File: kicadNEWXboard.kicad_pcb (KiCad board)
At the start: 2 copper layers, 89.7 x 38.1 mm, 24 parts, among them SW1 SW_Push, U1 ATmega32U4-AU, Y1 16MHz

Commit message: SVG
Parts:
- added D10: SOD-123, Diode_SMD:D_SOD-123, B.Cu at (71.3, 112.0)
- added D11: SOD-123, Diode_SMD:D_SOD-123, B.Cu at (90.4, 35.9)
- added D12: SOD-123, Diode_SMD:D_SOD-123, B.Cu at (90.5, 54.8)
- added D13: SOD-123, Diode_SMD:D_SOD-123, B.Cu at (100.0, 73.9)
- added D14: SOD-123, Diode_SMD:D_SOD-123, B.Cu at (90.4, 92.8)
- added D15: SOD-123, Diode_SMD:D_SOD-123, B.Cu at (90.4, 112.0)
- added D16: SOD-123, Diode_SMD:D_SOD-123, B.Cu at (109.4, 35.8)
- added D17: SOD-123, Diode_SMD:D_SOD-123, B.Cu at (109.5, 54.7)
- added D18: SOD-123, Diode_SMD:D_SOD-123, B.Cu at (118.9, 73.8)
- added D19: SOD-123, Diode_SMD:D_SOD-123, B.Cu at (109.4, 92.9)
- added D20: SOD-123, Diode_SMD:D_SOD-123, B.Cu at (114.2, 112.0)
- added D21: SOD-123, Diode_SMD:D_SOD-123, B.Cu at (128.5, 35.8)
- added D22: SOD-123, Diode_SMD:D_SOD-123, B.Cu at (128.5, 54.8)
- added D23: SOD-123, Diode_SMD:D_SOD-123, B.Cu at (138.0, 73.9)
- added D24: SOD-123, Diode_SMD:D_SOD-123, B.Cu at (128.5, 92.8)
- added D25: SOD-123, Diode_SMD:D_SOD-123, B.Cu at (138.0, 112.0)
- added D26: SOD-123, Diode_SMD:D_SOD-123, B.Cu at (147.5, 35.8)
- added D27: SOD-123, Diode_SMD:D_SOD-123, B.Cu at (147.5, 54.8)
- added D28: SOD-123, Diode_SMD:D_SOD-123, B.Cu at (157.0, 73.9)
- added D29: SOD-123, Diode_SMD:D_SOD-123, B.Cu at (147.5, 92.9)
- added D30: SOD-123, Diode_SMD:D_SOD-123, B.Cu at (161.7, 111.9)
- added D31: SOD-123, Diode_SMD:D_SOD-123, B.Cu at (166.6, 35.8)
- added D32: SOD-123, Diode_SMD:D_SOD-123, B.Cu at (166.6, 54.8)
- added D33: SOD-123, Diode_SMD:D_SOD-123, B.Cu at (176.1, 73.9)
- added D34: SOD-123, Diode_SMD:D_SOD-123, B.Cu at (166.7, 92.9)
- added D35: SOD-123, Diode_SMD:D_SOD-123, B.Cu at (185.6, 112.0)
- added D36: SOD-123, Diode_SMD:D_SOD-123, B.Cu at (185.6, 35.8)
- added D37: SOD-123, Diode_SMD:D_SOD-123, B.Cu at (185.6, 54.8)
- added D38: SOD-123, Diode_SMD:D_SOD-123, B.Cu at (195.0, 73.8)
- added D39: SOD-123, Diode_SMD:D_SOD-123, B.Cu at (185.6, 92.9)
- added D40: SOD-123, Diode_SMD:D_SOD-123, B.Cu at (204.7, 112.0)
- added D41: SOD-123, Diode_SMD:D_SOD-123, B.Cu at (204.7, 35.8)
- added D42: SOD-123, Diode_SMD:D_SOD-123, B.Cu at (204.7, 54.8)
- added D43: SOD-123, Diode_SMD:D_SOD-123, B.Cu at (214.2, 73.9)
- added D44: SOD-123, Diode_SMD:D_SOD-123, B.Cu at (204.7, 92.9)
- added D45: SOD-123, Diode_SMD:D_SOD-123, B.Cu at (223.7, 112.0)
- added D46: SOD-123, Diode_SMD:D_SOD-123, B.Cu at (223.7, 35.8)
- added D47: SOD-123, Diode_SMD:D_SOD-123, B.Cu at (223.7, 54.8)
- added D48: SOD-123, Diode_SMD:D_SOD-123, B.Cu at (223.7, 92.9)
- added D5: SOD-123, Diode_SMD:D_SOD-123, B.Cu at (61.9, 73.9)
- added D6: SOD-123, Diode_SMD:D_SOD-123, B.Cu at (52.3, 92.9)
- added D7: SOD-123, Diode_SMD:D_SOD-123, B.Cu at (52.3, 112.0)
- added D8: SOD-123, Diode_SMD:D_SOD-123, B.Cu at (80.8, 73.8)
- added D9: SOD-123, Diode_SMD:D_SOD-123, B.Cu at (71.3, 92.8)
- added MX10: MX-NoLED, MX_Alps_Hybrid:MX-1U, F.Cu at (63.5, 111.9)
- added MX11: MX-NoLED, MX_Alps_Hybrid:MX-1U, F.Cu at (82.5, 35.7)
- added MX12: MX-NoLED, MX_Alps_Hybrid:MX-1U, F.Cu at (82.5, 54.8)
- added MX13: MX-NoLED, MX_Alps_Hybrid:MX-1U, F.Cu at (92.1, 73.8)
- added MX14: MX-NoLED, MX_Alps_Hybrid:MX-1U, F.Cu at (82.5, 92.9)
- added MX15: MX-NoLED, MX_Alps_Hybrid:MX-1U, F.Cu at (82.5, 111.9)
- added MX16: MX-NoLED, MX_Alps_Hybrid:MX-1U, F.Cu at (101.6, 35.7)
- added MX17: MX-NoLED, MX_Alps_Hybrid:MX-1U, F.Cu at (101.6, 54.8)
- added MX18: MX-NoLED, MX_Alps_Hybrid:MX-1U, F.Cu at (111.1, 73.8)
- added MX19: MX-NoLED, MX_Alps_Hybrid:MX-1U, F.Cu at (101.6, 92.9)
- added MX20: MX-NoLED, MX_Alps_Hybrid:MX-1U, F.Cu at (106.4, 111.9)
- added MX21: MX-NoLED, MX_Alps_Hybrid:MX-1U, F.Cu at (120.7, 35.7)
- added MX22: MX-NoLED, MX_Alps_Hybrid:MX-1U, F.Cu at (120.7, 54.8)
- added MX23: MX-NoLED, MX_Alps_Hybrid:MX-1U, F.Cu at (130.2, 73.8)
- added MX24: MX-NoLED, MX_Alps_Hybrid:MX-1U, F.Cu at (120.7, 92.9)
- added MX25: MX-NoLED, MX_Alps_Hybrid:MX-1U, F.Cu at (130.2, 111.9)
- added MX26: MX-NoLED, MX_Alps_Hybrid:MX-1U, F.Cu at (139.7, 35.7)
- added MX27: MX-NoLED, MX_Alps_Hybrid:MX-1U, F.Cu at (139.7, 54.8)
- added MX28: MX-NoLED, MX_Alps_Hybrid:MX-1U, F.Cu at (149.2, 73.8)
- added MX29: MX-NoLED, MX_Alps_Hybrid:MX-1U, F.Cu at (139.7, 92.9)
- added MX30: MX-NoLED, MX_Alps_Hybrid:MX-1U, F.Cu at (154.0, 111.9)
- added MX31: MX-NoLED, MX_Alps_Hybrid:MX-1U, F.Cu at (158.8, 35.7)
- added MX32: MX-NoLED, MX_Alps_Hybrid:MX-1U, F.Cu at (158.8, 54.8)
- added MX33: MX-NoLED, MX_Alps_Hybrid:MX-1U, F.Cu at (168.3, 73.8)
- added MX34: MX-NoLED, MX_Alps_Hybrid:MX-1U, F.Cu at (158.8, 92.9)
- added MX35: MX-NoLED, MX_Alps_Hybrid:MX-1U, F.Cu at (177.8, 111.9)
- added MX36: MX-NoLED, MX_Alps_Hybrid:MX-1U, F.Cu at (177.8, 35.7)
- added MX37: MX-NoLED, MX_Alps_Hybrid:MX-1U, F.Cu at (177.8, 54.8)
- added MX38: MX-NoLED, MX_Alps_Hybrid:MX-1U, F.Cu at (187.3, 73.8)
- added MX39: MX-NoLED, MX_Alps_Hybrid:MX-1U, F.Cu at (177.8, 92.9)
- added MX40: MX-NoLED, MX_Alps_Hybrid:MX-1U, F.Cu at (196.8, 111.9)
- added MX41: MX-NoLED, MX_Alps_Hybrid:MX-1U, F.Cu at (196.8, 35.7)
- added MX42: MX-NoLED, MX_Alps_Hybrid:MX-1U, F.Cu at (196.8, 54.8)
- added MX43: MX-NoLED, MX_Alps_Hybrid:MX-1U, F.Cu at (206.4, 73.8)
- added MX44: MX-NoLED, MX_Alps_Hybrid:MX-1U, F.Cu at (196.8, 92.9)
- added MX45: MX-NoLED, MX_Alps_Hybrid:MX-1U, F.Cu at (215.9, 111.9)
- added MX46: MX-NoLED, MX_Alps_Hybrid:MX-1U, F.Cu at (215.9, 35.7)
- added MX47: MX-NoLED, MX_Alps_Hybrid:MX-1U, F.Cu at (215.9, 54.8)
- added MX48: MX-NoLED, MX_Alps_Hybrid:MX-1U, F.Cu at (215.9, 92.9)
- added MX5: MX-NoLED, MX_Alps_Hybrid:MX-1U, F.Cu at (54.0, 73.8)
- added MX6: MX-NoLED, MX_Alps_Hybrid:MX-1U, F.Cu at (44.5, 92.9)
- added MX7: MX-NoLED, MX_Alps_Hybrid:MX-1U, F.Cu at (44.5, 111.9)
- added MX8: MX-NoLED, MX_Alps_Hybrid:MX-1U, F.Cu at (73.0, 73.8)
- added MX9: MX-NoLED, MX_Alps_Hybrid:MX-1U, F.Cu at (63.5, 92.9)
- moved MX3 152.9 mm to (63.5, 35.7)
- moved MX4 152.9 mm to (63.5, 54.8)
- moved MX1 152.9 mm to (44.5, 35.7)
- moved MX2 152.9 mm to (44.5, 54.8)
- moved D4 138.3 mm to (71.4, 54.8)
- moved D1 138.1 mm to (52.4, 35.8)
- moved D3 138.1 mm to (71.4, 35.8)
- moved D2 137.9 mm to (52.4, 54.8)
- moved USB1 105.4 mm to (223.6, 134.5), turned to 180 degrees
- moved R1 96.6 mm to (210.4, 149.2), turned to 180 degrees
- moved SW1 93.6 mm to (220.9, 147.4), turned to 270 degrees
- moved R2 90.5 mm to (210.4, 145.5), turned to 180 degrees
- moved F1 90.5 mm to (211.3, 138.7), turned to 0 degrees
- moved R3 74.3 mm to (188.2, 154.6), turned to 180 degrees
- moved C6 70.5 mm to (193.2, 153.4)
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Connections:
- U1 pad 18: Net-(U1-Pad18) -> COL0
- U1 pad 19: Net-(U1-Pad19) -> COL1
- U1 pad 20: Net-(U1-Pad20) -> COL2
- U1 pad 21: Net-(U1-Pad21) -> COL3
- U1 pad 22: Net-(U1-Pad22) -> COL4
- U1 pad 26: Net-(U1-Pad26) -> COL5
- U1 pad 27: Net-(U1-Pad27) -> COL6
- U1 pad 28: Net-(U1-Pad28) -> COL7
- U1 pad 29: Net-(U1-Pad29) -> COL8
- U1 pad 30: Net-(U1-Pad30) -> COL9
- U1 pad 37: Net-(U1-Pad37) -> ROW0
- U1 pad 38: Net-(U1-Pad38) -> ROW1
- U1 pad 39: Net-(U1-Pad39) -> ROW2
- U1 pad 40: Net-(U1-Pad40) -> ROW3
- U1 pad 41: Net-(U1-Pad41) -> ROW4
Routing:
- net ROW0: track 19.6 -> 303.5 mm, vias 0 -> 6
- net COL2: track 0.00 -> 227.0 mm, vias 0 -> 1
- net ROW4: track 0.00 -> 220.8 mm, vias 0 -> 4
- net COL0: track 38.5 -> 256.6 mm, vias 0 -> 1
- net COL1: track 29.3 -> 236.8 mm, vias 0 -> 1
- net COL3: track 0.00 -> 195.1 mm, vias 0 -> 1
- net COL4: track 0.00 -> 173.6 mm, vias 0 -> 1
- net COL5: track 0.00 -> 155.6 mm, vias 0 -> 3
- net COL6: track 0.00 -> 132.9 mm, vias 0 -> 1
- net COL8: track 0.00 -> 129.7 mm, vias 0 -> 2
- net COL7: track 0.00 -> 125.4 mm, vias 0 -> 1
- net COL9: track 0.00 -> 110.8 mm, vias 0 -> 2
- net ROW2: track 0.00 -> 85.1 mm, vias 0 -> 6
- net ROW1: track 20.0 -> 101.9 mm, vias 0 -> 6
- net ROW3: track 0.00 -> 63.9 mm, vias 0 -> 6
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- added copper zone on B.Cu, net GND
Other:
- board size 89.7 x 38.1 mm -> 190.5 x 131.8 mm
- board text added: "newk-board-01 so cool and so awesome wow wow wow"

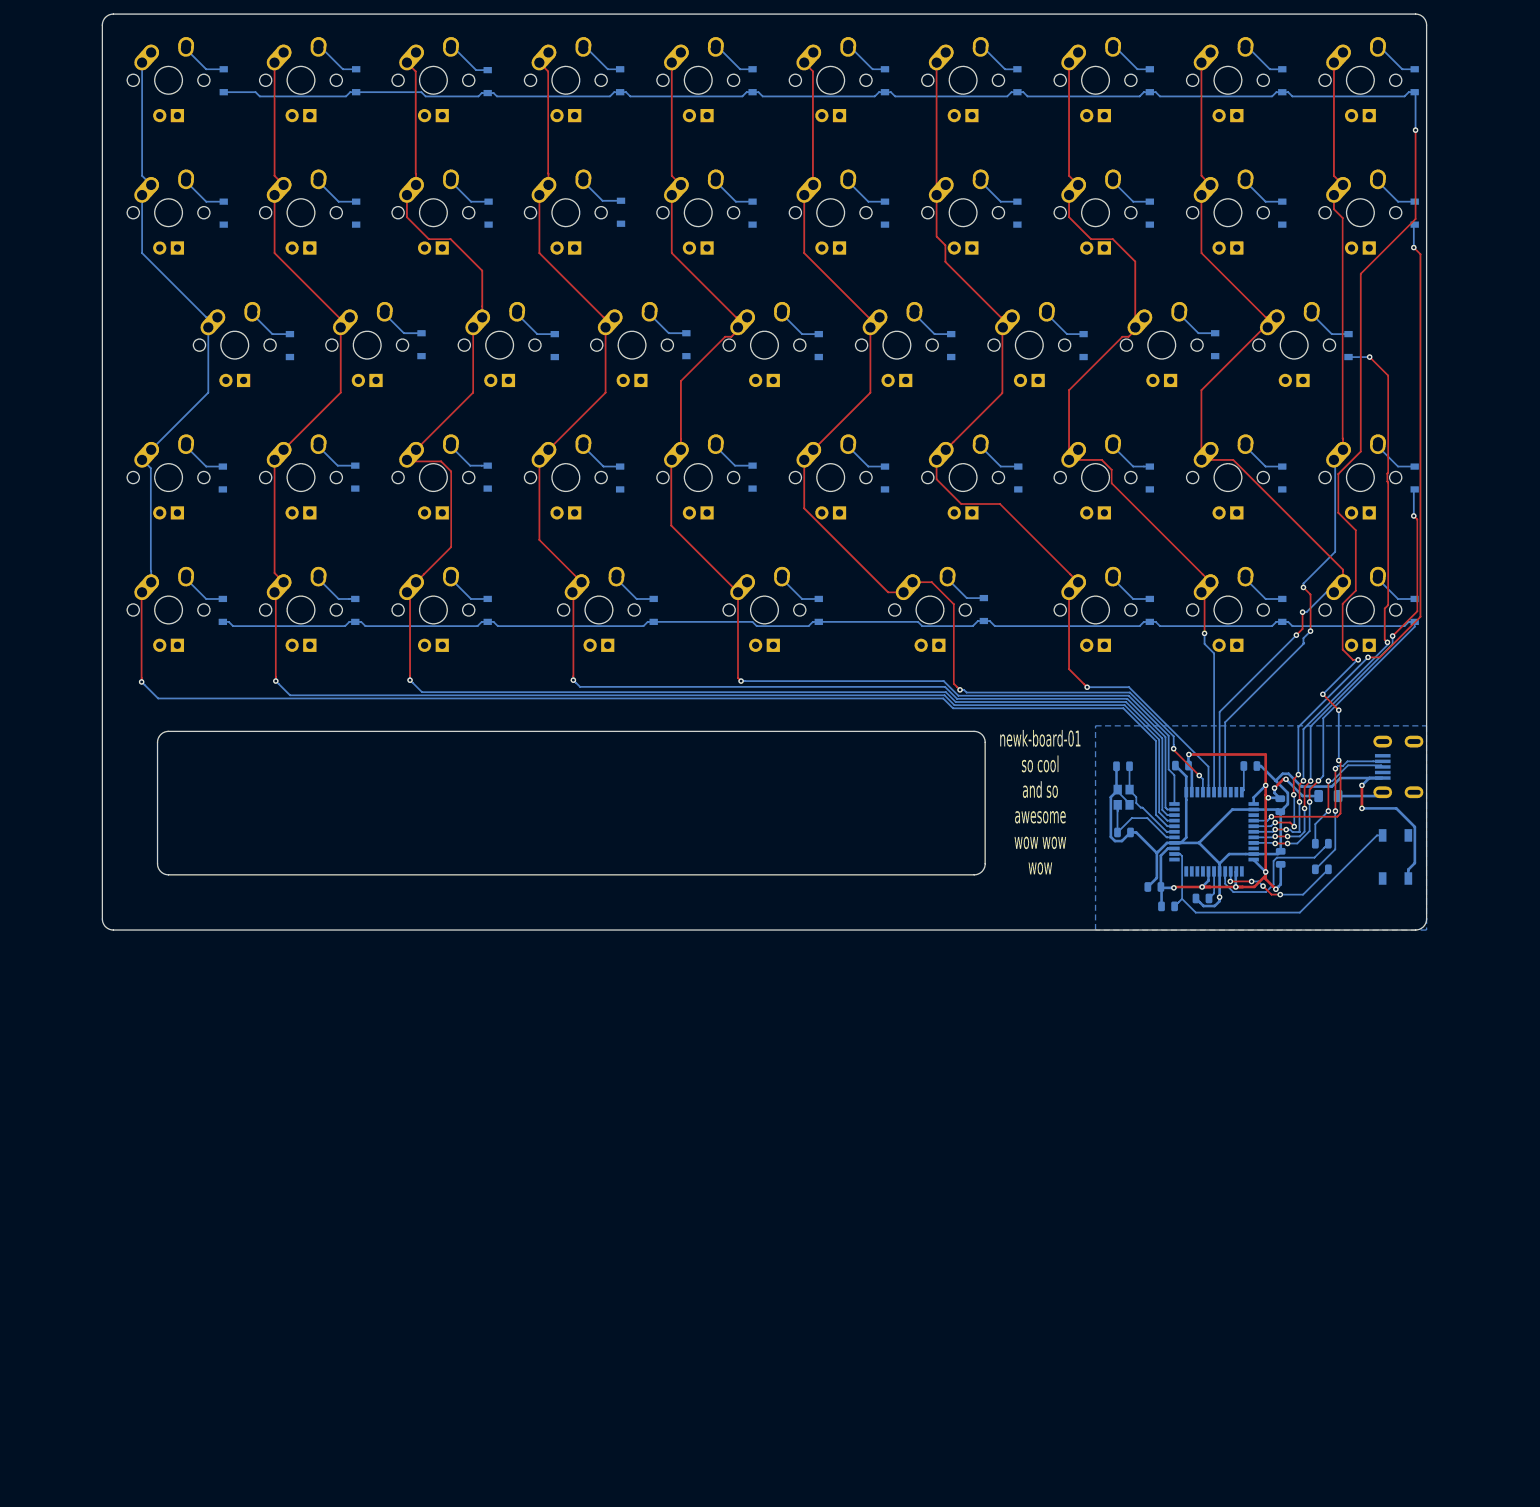
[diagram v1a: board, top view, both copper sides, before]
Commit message: slimming electronics
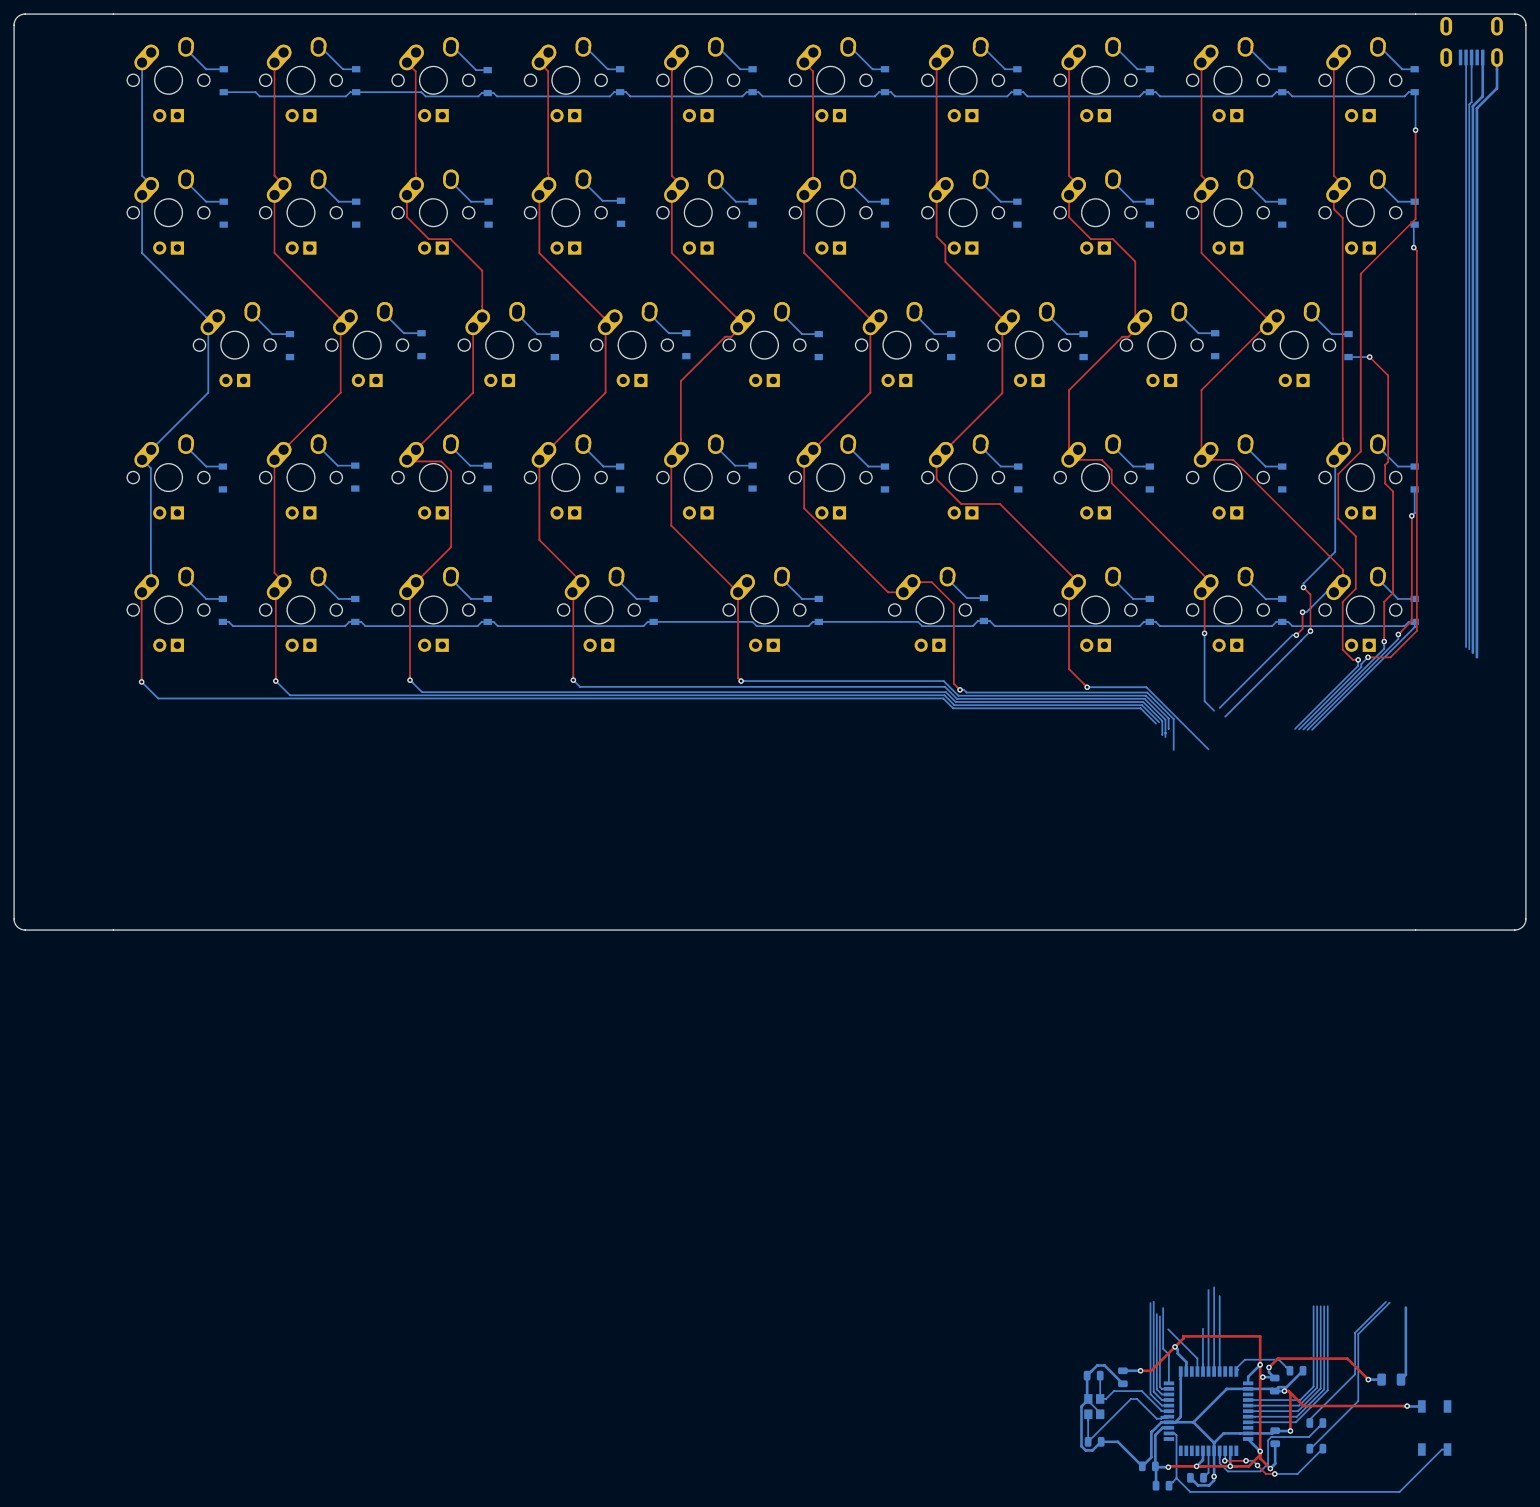
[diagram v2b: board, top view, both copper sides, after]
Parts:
- moved USB1 106.9 mm to (231.9, 27.9), turned to 270 degrees
- moved C1 88.4 mm to (181.7, 222.3), turned to 270 degrees
- moved C3 87.8 mm to (177.5, 222.1)
- moved C4 87.8 mm to (177.7, 231.6)
- moved Y1 87.8 mm to (177.6, 226.5)
- moved R4 87.2 mm to (206.7, 221.4)
- moved F1 84.4 mm to (220.3, 222.6)
- moved C2 83.3 mm to (185.5, 235.1)
- moved C5 83.3 mm to (203.6, 223.3)
- moved C6 83.3 mm to (192.4, 236.8)
- moved C7 83.3 mm to (203.6, 230.9)
- moved R1 83.3 mm to (209.6, 232.6)
- moved R2 83.3 mm to (209.6, 228.9)
- moved R3 83.3 mm to (187.4, 237.9)
- moved U1 83.3 mm to (194.1, 227.2)
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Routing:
- net VCC: track 6.64 -> 98.1 mm
- net D+: track 18.6 -> 107.2 mm, vias 2 -> 0
- net D-: track 22.9 -> 110.6 mm, vias 2 -> 0
- net GND: track 139.6 -> 210.4 mm, vias 3 -> 4
- net +5V: track 91.1 -> 110.3 mm, vias 10 -> 11
- net Net-(R3-Pad1): track 43.2 -> 51.2 mm
- net Net-(C4-Pad1): track 15.1 -> 21.5 mm
- net Net-(R4-Pad2): track 3.88 -> 9.75 mm
- net ROW0: track 303.5 -> 300.7 mm, vias 6 -> 2
- net ROW1: track 101.9 -> 104.4 mm, vias 6 -> 2
- net Net-(C3-Pad1): track 12.9 -> 15.1 mm
- net ROW2: track 85.1 -> 87.3 mm, vias 6 -> 2
- net ROW4: track 220.8 -> 222.7 mm, vias 4 -> 0
- net ROW3: track 63.9 -> 65.5 mm, vias 6 -> 2
- net COL3: track 195.1 -> 196.5 mm
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- removed copper zone on B.Cu, net GND
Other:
- board size 190.5 x 131.8 mm -> 217.5 x 131.8 mm
- board text removed: "newk-board-01 so cool and so awesome wow wow wow"
